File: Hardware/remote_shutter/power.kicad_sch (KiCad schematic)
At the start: 0 parts

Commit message: Added power & comms.
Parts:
- added C?: 10u, symbol Device:C_Polarized_Small
- added C?: 22u, symbol Device:C_Polarized_Small
- added J?: Conn_01x02_Male, symbol Connector:Conn_01x02_Male
- added U?: AZ1117-3.3, symbol Regulator_Linear:AZ1117-3.3
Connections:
- new net: C?.1, J?.1 (Pin_1), U?.3 (VI)
- new net 3V3: C?.1, U?.2 (VO)
- new net GND: C?.2, C?.2, J?.2 (Pin_2), U?.1 (GND)
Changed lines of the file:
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@@
 (kicad_sch (version 20211123) (generator eeschema)
   (paper "A4")
+  (junction (at 157.48 88.9) (diameter 0) (color 0 0 0 0)
+  )
+  (junction (at 132.08 88.9) (diameter 0) (color 0 0 0 0)
+  )
+  (wire (pts (xy 166.37 91.44) (xy 167.64 91.44))
+    (stroke (width 0) (type default) (color 0 0 0 0))
+  )
+  (wire (pts (xy 132.08 88.9) (xy 132.08 91.44))
+    (stroke (width 0) (type default) (color 0 0 0 0))
+  )
+  (wire (pts (xy 120.65 88.9) (xy 132.08 88.9))
+    (stroke (width 0) (type default) (color 0 0 0 0))
+  )
+  (wire (pts (xy 157.48 91.44) (xy 157.48 88.9))
+    (stroke (width 0) (type default) (color 0 0 0 0))
+  )
+  (wire (pts (xy 153.67 88.9) (xy 157.48 88.9))
+    (stroke (width 0) (type default) (color 0 0 0 0))
+  )
+  (wire (pts (xy 132.08 88.9) (xy 138.43 88.9))
+    (stroke (width 0) (type default) (color 0 0 0 0))
+  )
+  (wire (pts (xy 120.65 91.44) (xy 124.46 91.44))
+    (stroke (width 0) (type default) (color 0 0 0 0))
+  )
+  (wire (pts (xy 166.37 92.71) (xy 166.37 91.44))
+    (stroke (width 0) (type default) (color 0 0 0 0))
+  )
+  (wire (pts (xy 157.48 88.9) (xy 167.64 88.9))
+    (stroke (width 0) (type default) (color 0 0 0 0))
+  )
+  (hierarchical_label "3V3" (shape input) (at 167.64 88.9 0)
+    (effects (font (size 1.27 1.27)) (justify left))
+  )
+  (hierarchical_label "GND" (shape input) (at 167.64 91.44 0)
+    (effects (font (size 1.27 1.27)) (justify left))
+  )
+  (symbol (lib_id "power:GND") (at 166.37 92.71 0) (unit 1)
+    (in_bom yes) (on_board yes) (fields_autoplaced)
+    (property "Reference" "#PWR?" (id 0) (at 166.37 99.06 0)
+      (effects (font (size 1.27 1.27)) hide)
+    )
+    (property "Value" "GND" (id 1) (at 166.37 97.79 0))
+    (property "Footprint" "" (id 2) (at 166.37 92.71 0)
+      (effects (font (size 1.27 1.27)) hide)
+    )
+    (property "Datasheet" "" (id 3) (at 166.37 92.71 0)
+      (effects (font (size 1.27 1.27)) hide)
+    )
+    (pin "1")
+  )
+  (symbol (lib_id "power:GND") (at 132.08 96.52 0) (unit 1)
+    (in_bom yes) (on_board yes) (fields_autoplaced)
+    (property "Reference" "#PWR?" (id 0) (at 132.08 102.87 0)
+      (effects (font (size 1.27 1.27)) hide)
+    )
+    (property "Value" "GND" (id 1) (at 132.08 101.6 0))
+    (property "Footprint" "" (id 2) (at 132.08 96.52 0)
+      (effects (font (size 1.27 1.27)) hide)
+    )
+    (property "Datasheet" "" (id 3) (at 132.08 96.52 0)
+      (effects (font (size 1.27 1.27)) hide)
+    )
+    (pin "1")
+  )
+  (symbol (lib_id "Device:C_Polarized_Small") (at 132.08 93.98 0) (unit 1)
+    (in_bom yes) (on_board yes) (fields_autoplaced)
+    (property "Reference" "C?" (id 0) (at 134.62 92.1638 0)
+      (effects (font (size 1.27 1.27)) (justify left))
+    )
+    (property "Value" "10u" (id 1) (at 134.62 94.7038 0)
+      (effects (font (size 1.27 1.27)) (justify left))
+    )
+    (property "Footprint" "" (id 2) (at 132.08 93.98 0)
+      (effects (font (size 1.27 1.27)) hide)
+    )
+    (property "Datasheet" "~" (id 3) (at 132.08 93.98 0)
+      (effects (font (size 1.27 1.27)) hide)
+    )
+    (pin "1")
+    (pin "2")
+  )
+  (symbol (lib_id "power:GND") (at 124.46 91.44 0) (unit 1)
+    (in_bom yes) (on_board yes) (fields_autoplaced)
+    (property "Reference" "#PWR?" (id 0) (at 124.46 97.79 0)
+      (effects (font (size 1.27 1.27)) hide)
+    )
+    (property "Value" "GND" (id 1) (at 124.46 96.52 0))
+    (property "Footprint" "" (id 2) (at 124.46 91.44 0)
+      (effects (font (size 1.27 1.27)) hide)
+    )
+    (property "Datasheet" "" (id 3) (at 124.46 91.44 0)
+      (effects (font (size 1.27 1.27)) hide)
+    )
+    (pin "1")
+  )
+  (symbol (lib_id "power:GND") (at 146.05 96.52 0) (unit 1)
+    (in_bom yes) (on_board yes) (fields_autoplaced)
+    (property "Reference" "#PWR?" (id 0) (at 146.05 102.87 0)
+      (effects (font (size 1.27 1.27)) hide)
+    )
+    (property "Value" "GND" (id 1) (at 146.05 101.6 0))
+    (property "Footprint" "" (id 2) (at 146.05 96.52 0)
+      (effects (font (size 1.27 1.27)) hide)
+    )
+    (property "Datasheet" "" (id 3) (at 146.05 96.52 0)
+      (effects (font (size 1.27 1.27)) hide)
+    )
+    (pin "1")
+  )
+  (symbol (lib_id "Regulator_Linear:AZ1117-3.3") (at 146.05 88.9 0) (unit 1)
+    (in_bom yes) (on_board yes) (fields_autoplaced)
+    (property "Reference" "U?" (id 0) (at 146.05 81.28 0))
+    (property "Value" "AZ1117-3.3" (id 1) (at 146.05 83.82 0))
+    (property "Footprint" "" (id 2) (at 146.05 82.55 0)
+      (effects (font (size 1.27 1.27) italic) hide)
+    )
+    (property "Datasheet" "https://www.diodes.com/assets/Datasheets/AZ1117.pdf" (id 3) (at 146.05 88.9 0)
+      (effects (font (size 1.27 1.27)) hide)
+    )
+    (pin "1")
+    (pin "2")
+    (pin "3")
+  )
+  (symbol (lib_id "power:GND") (at 157.48 96.52 0) (unit 1)
+    (in_bom yes) (on_board yes) (fields_autoplaced)
+    (property "Reference" "#PWR?" (id 0) (at 157.48 102.87 0)
+      (effects (font (size 1.27 1.27)) hide)
+    )
+    (property "Value" "GND" (id 1) (at 157.48 101.6 0))
+    (property "Footprint" "" (id 2) (at 157.48 96.52 0)
+      (effects (font (size 1.27 1.27)) hide)
+    )
+    (property "Datasheet" "" (id 3) (at 157.48 96.52 0)
+      (effects (font (size 1.27 1.27)) hide)
+    )
+    (pin "1")
+  )
+  (symbol (lib_id "Device:C_Polarized_Small") (at 157.48 93.98 0) (unit 1)
+    (in_bom yes) (on_board yes) (fields_autoplaced)
+    (property "Reference" "C?" (id 0) (at 160.02 92.1638 0)
+      (effects (font (size 1.27 1.27)) (justify left))
+    )
+    (property "Value" "22u" (id 1) (at 160.02 94.7038 0)
+      (effects (font (size 1.27 1.27)) (justify left))
+    )
+    (property "Footprint" "" (id 2) (at 157.48 93.98 0)
+      (effects (font (size 1.27 1.27)) hide)
+    )
+    (property "Datasheet" "~" (id 3) (at 157.48 93.98 0)
+      (effects (font (size 1.27 1.27)) hide)
+    )
+    (pin "1")
+    (pin "2")
+  )
+  (symbol (lib_id "Connector:Conn_01x02_Male") (at 115.57 88.9 0) (unit 1)
+    (in_bom yes) (on_board yes) (fields_autoplaced)
+    (property "Reference" "J?" (id 0) (at 116.205 83.82 0))
+    (property "Value" "Conn_01x02_Male" (id 1) (at 116.205 86.36 0))
+    (property "Footprint" "" (id 2) (at 115.57 88.9 0)
+      (effects (font (size 1.27 1.27)) hide)
+    )
+    (property "Datasheet" "~" (id 3) (at 115.57 88.9 0)
+      (effects (font (size 1.27 1.27)) hide)
+    )
+    (pin "1")
+    (pin "2")
+  )
 )

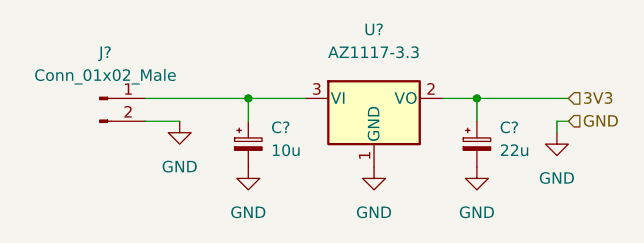
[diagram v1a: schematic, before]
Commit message: Added missing footprints. First PCB export.
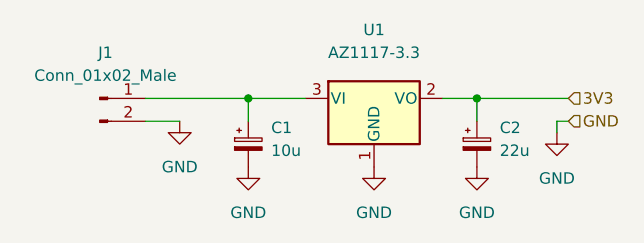
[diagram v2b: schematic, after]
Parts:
- C1, C2: renamed from C?; footprint (none) -> Capacitor_Tantalum_SMD:CP_EIA-3528-21_Kemet-B_Pad1.50x2.35mm_HandSolder
- gave numbers to parts that had none: 2
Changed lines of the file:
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@@
   (symbol (lib_id "power:GND") (at 166.37 92.71 0) (unit 1)
     (in_bom yes) (on_board yes) (fields_autoplaced)
-    (property "Reference" "#PWR?" (id 0) (at 166.37 99.06 0)
+    (property "Reference" "#PWR0102" (id 0) (at 166.37 99.06 0)
       (effects (font (size 1.27 1.27)) hide)
     )
@@
   (symbol (lib_id "power:GND") (at 132.08 96.52 0) (unit 1)
     (in_bom yes) (on_board yes) (fields_autoplaced)
-    (property "Reference" "#PWR?" (id 0) (at 132.08 102.87 0)
+    (property "Reference" "#PWR0104" (id 0) (at 132.08 102.87 0)
       (effects (font (size 1.27 1.27)) hide)
     )
@@
   (symbol (lib_id "Device:C_Polarized_Small") (at 132.08 93.98 0) (unit 1)
     (in_bom yes) (on_board yes) (fields_autoplaced)
-    (property "Reference" "C?" (id 0) (at 134.62 92.1638 0)
+    (property "Reference" "C1" (id 0) (at 134.62 92.1638 0)
       (effects (font (size 1.27 1.27)) (justify left))
     )
@@
       (effects (font (size 1.27 1.27)) (justify left))
     )
-    (property "Footprint" "" (id 2) (at 132.08 93.98 0)
+    (property "Footprint" "Capacitor_Tantalum_SMD:CP_EIA-3528-21_Kemet-B_Pad1.50x2.35mm_HandSolder" (id 2) (at 132.08 93.98 0)
       (effects (font (size 1.27 1.27)) hide)
     )
@@
   (symbol (lib_id "power:GND") (at 124.46 91.44 0) (unit 1)
     (in_bom yes) (on_board yes) (fields_autoplaced)
-    (property "Reference" "#PWR?" (id 0) (at 124.46 97.79 0)
+    (property "Reference" "#PWR0105" (id 0) (at 124.46 97.79 0)
       (effects (font (size 1.27 1.27)) hide)
     )
@@
   (symbol (lib_id "power:GND") (at 146.05 96.52 0) (unit 1)
     (in_bom yes) (on_board yes) (fields_autoplaced)
-    (property "Reference" "#PWR?" (id 0) (at 146.05 102.87 0)
+    (property "Reference" "#PWR0103" (id 0) (at 146.05 102.87 0)
       (effects (font (size 1.27 1.27)) hide)
     )
@@
   (symbol (lib_id "Regulator_Linear:AZ1117-3.3") (at 146.05 88.9 0) (unit 1)
     (in_bom yes) (on_board yes) (fields_autoplaced)
-    (property "Reference" "U?" (id 0) (at 146.05 81.28 0))
+    (property "Reference" "U1" (id 0) (at 146.05 81.28 0))
     (property "Value" "AZ1117-3.3" (id 1) (at 146.05 83.82 0))
     (property "Footprint" "" (id 2) (at 146.05 82.55 0)
@@
   (symbol (lib_id "power:GND") (at 157.48 96.52 0) (unit 1)
     (in_bom yes) (on_board yes) (fields_autoplaced)
-    (property "Reference" "#PWR?" (id 0) (at 157.48 102.87 0)
+    (property "Reference" "#PWR0101" (id 0) (at 157.48 102.87 0)
       (effects (font (size 1.27 1.27)) hide)
     )
@@
   (symbol (lib_id "Device:C_Polarized_Small") (at 157.48 93.98 0) (unit 1)
     (in_bom yes) (on_board yes) (fields_autoplaced)
-    (property "Reference" "C?" (id 0) (at 160.02 92.1638 0)
+    (property "Reference" "C2" (id 0) (at 160.02 92.1638 0)
       (effects (font (size 1.27 1.27)) (justify left))
     )
@@
       (effects (font (size 1.27 1.27)) (justify left))
     )
-    (property "Footprint" "" (id 2) (at 157.48 93.98 0)
+    (property "Footprint" "Capacitor_Tantalum_SMD:CP_EIA-3528-21_Kemet-B_Pad1.50x2.35mm_HandSolder" (id 2) (at 157.48 93.98 0)
       (effects (font (size 1.27 1.27)) hide)
     )
@@
   (symbol (lib_id "Connector:Conn_01x02_Male") (at 115.57 88.9 0) (unit 1)
     (in_bom yes) (on_board yes) (fields_autoplaced)
-    (property "Reference" "J?" (id 0) (at 116.205 83.82 0))
+    (property "Reference" "J1" (id 0) (at 116.205 83.82 0))
     (property "Value" "Conn_01x02_Male" (id 1) (at 116.205 86.36 0))
     (property "Footprint" "" (id 2) (at 115.57 88.9 0)

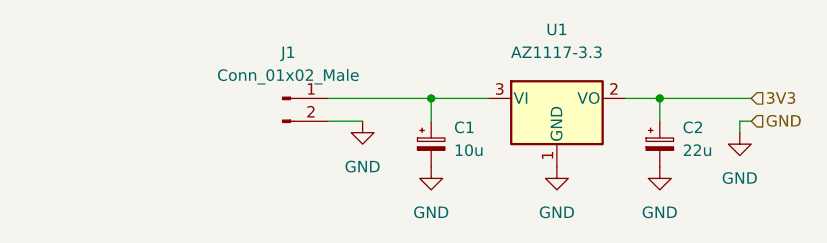
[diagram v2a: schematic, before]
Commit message: Started routing. Added power switch.
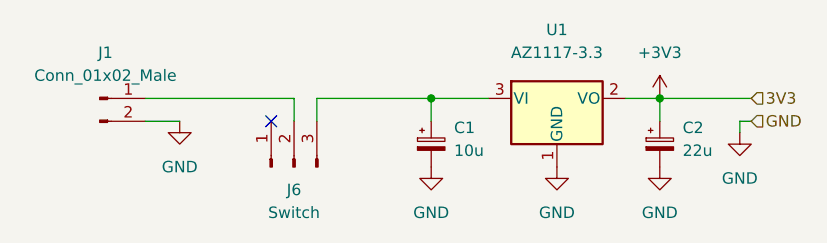
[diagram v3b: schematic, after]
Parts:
- added J6: Switch, Connector_PinHeader_2.54mm:PinHeader_1x03_P2.54mm_Vertical, symbol Connector:Conn_01x03_Male
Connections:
- net at C1.1, U1.3 (VI): now also J6.3 (Pin_3); no longer J1.1 (Pin_1)
- net 3V3 renamed +3V3
- new net: J1.1 (Pin_1), J6.2 (Pin_2)
- no-connect marks 0 -> 1
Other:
- moved on the sheet: J1
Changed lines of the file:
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@@
   (junction (at 132.08 88.9) (diameter 0) (color 0 0 0 0)
   )
+  (no_connect (at 114.3 91.44))
+  (wire (pts (xy 119.38 88.9) (xy 132.08 88.9))
+    (stroke (width 0) (type default) (color 0 0 0 0))
+  )
   (wire (pts (xy 166.37 91.44) (xy 167.64 91.44))
     (stroke (width 0) (type default) (color 0 0 0 0))
@@
     (stroke (width 0) (type default) (color 0 0 0 0))
   )
-  (wire (pts (xy 120.65 88.9) (xy 132.08 88.9))
-    (stroke (width 0) (type default) (color 0 0 0 0))
-  )
   (wire (pts (xy 157.48 91.44) (xy 157.48 88.9))
     (stroke (width 0) (type default) (color 0 0 0 0))
   )
+  (wire (pts (xy 116.84 88.9) (xy 116.84 91.44))
+    (stroke (width 0) (type default) (color 0 0 0 0))
+  )
   (wire (pts (xy 153.67 88.9) (xy 157.48 88.9))
     (stroke (width 0) (type default) (color 0 0 0 0))
@@
     (stroke (width 0) (type default) (color 0 0 0 0))
   )
-  (wire (pts (xy 120.65 91.44) (xy 124.46 91.44))
+  (wire (pts (xy 100.33 91.44) (xy 104.14 91.44))
     (stroke (width 0) (type default) (color 0 0 0 0))
   )
   (wire (pts (xy 166.37 92.71) (xy 166.37 91.44))
+    (stroke (width 0) (type default) (color 0 0 0 0))
+  )
+  (wire (pts (xy 100.33 88.9) (xy 116.84 88.9))
+    (stroke (width 0) (type default) (color 0 0 0 0))
+  )
+  (wire (pts (xy 119.38 91.44) (xy 119.38 88.9))
     (stroke (width 0) (type default) (color 0 0 0 0))
   )
@@
     (effects (font (size 1.27 1.27)) (justify left))
   )
+  (symbol (lib_id "power:+3V3") (at 157.48 88.9 0) (unit 1)
+    (in_bom yes) (on_board yes) (fields_autoplaced)
+    (property "Reference" "#PWR?" (id 0) (at 157.48 92.71 0)
+      (effects (font (size 1.27 1.27)) hide)
+    )
+    (property "Value" "+3V3" (id 1) (at 157.48 83.82 0))
+    (property "Footprint" "" (id 2) (at 157.48 88.9 0)
+      (effects (font (size 1.27 1.27)) hide)
+    )
+    (property "Datasheet" "" (id 3) (at 157.48 88.9 0)
+      (effects (font (size 1.27 1.27)) hide)
+    )
+    (pin "1")
+  )
   (symbol (lib_id "power:GND") (at 166.37 92.71 0) (unit 1)
     (in_bom yes) (on_board yes) (fields_autoplaced)
@@
     (pin "2")
   )
-  (symbol (lib_id "power:GND") (at 124.46 91.44 0) (unit 1)
-    (in_bom yes) (on_board yes) (fields_autoplaced)
-    (property "Reference" "#PWR0105" (id 0) (at 124.46 97.79 0)
-      (effects (font (size 1.27 1.27)) hide)
-    )
-    (property "Value" "GND" (id 1) (at 124.46 96.52 0))
-    (property "Footprint" "" (id 2) (at 124.46 91.44 0)
-      (effects (font (size 1.27 1.27)) hide)
-    )
-    (property "Datasheet" "" (id 3) (at 124.46 91.44 0)
+  (symbol (lib_id "power:GND") (at 104.14 91.44 0) (unit 1)
+    (in_bom yes) (on_board yes) (fields_autoplaced)
+    (property "Reference" "#PWR0105" (id 0) (at 104.14 97.79 0)
+      (effects (font (size 1.27 1.27)) hide)
+    )
+    (property "Value" "GND" (id 1) (at 104.14 96.52 0))
+    (property "Footprint" "" (id 2) (at 104.14 91.44 0)
+      (effects (font (size 1.27 1.27)) hide)
+    )
+    (property "Datasheet" "" (id 3) (at 104.14 91.44 0)
       (effects (font (size 1.27 1.27)) hide)
     )
@@
     (pin "2")
   )
-  (symbol (lib_id "Connector:Conn_01x02_Male") (at 115.57 88.9 0) (unit 1)
-    (in_bom yes) (on_board yes) (fields_autoplaced)
-    (property "Reference" "J1" (id 0) (at 116.205 83.82 0))
-    (property "Value" "Conn_01x02_Male" (id 1) (at 116.205 86.36 0))
-    (property "Footprint" "" (id 2) (at 115.57 88.9 0)
-      (effects (font (size 1.27 1.27)) hide)
-    )
-    (property "Datasheet" "~" (id 3) (at 115.57 88.9 0)
-      (effects (font (size 1.27 1.27)) hide)
-    )
+  (symbol (lib_id "Connector:Conn_01x03_Male") (at 116.84 96.52 90) (unit 1)
+    (in_bom yes) (on_board yes) (fields_autoplaced)
+    (property "Reference" "J6" (id 0) (at 116.84 99.06 90))
+    (property "Value" "Switch" (id 1) (at 116.84 101.6 90))
+    (property "Footprint" "Connector_PinHeader_2.54mm:PinHeader_1x03_P2.54mm_Vertical" (id 2) (at 116.84 96.52 0)
+      (effects (font (size 1.27 1.27)) hide)
+    )
+    (property "Datasheet" "~" (id 3) (at 116.84 96.52 0)
+      (effects (font (size 1.27 1.27)) hide)
+    )
+    (pin "1")
+    (pin "2")
+    (pin "3")
+  )
+  (symbol (lib_id "Connector:Conn_01x02_Male") (at 95.25 88.9 0) (unit 1)
+    (in_bom yes) (on_board yes) (fields_autoplaced)
+    (property "Reference" "J1" (id 0) (at 95.885 83.82 0))
+    (property "Value" "Conn_01x02_Male" (id 1) (at 95.885 86.36 0))
+    (property "Footprint" "" (id 2) (at 95.25 88.9 0)
+      (effects (font (size 1.27 1.27)) hide)
+    )
+    (property "Datasheet" "~" (id 3) (at 95.25 88.9 0)
+      (effects (font (size 1.27 1.27)) hide)
+    )

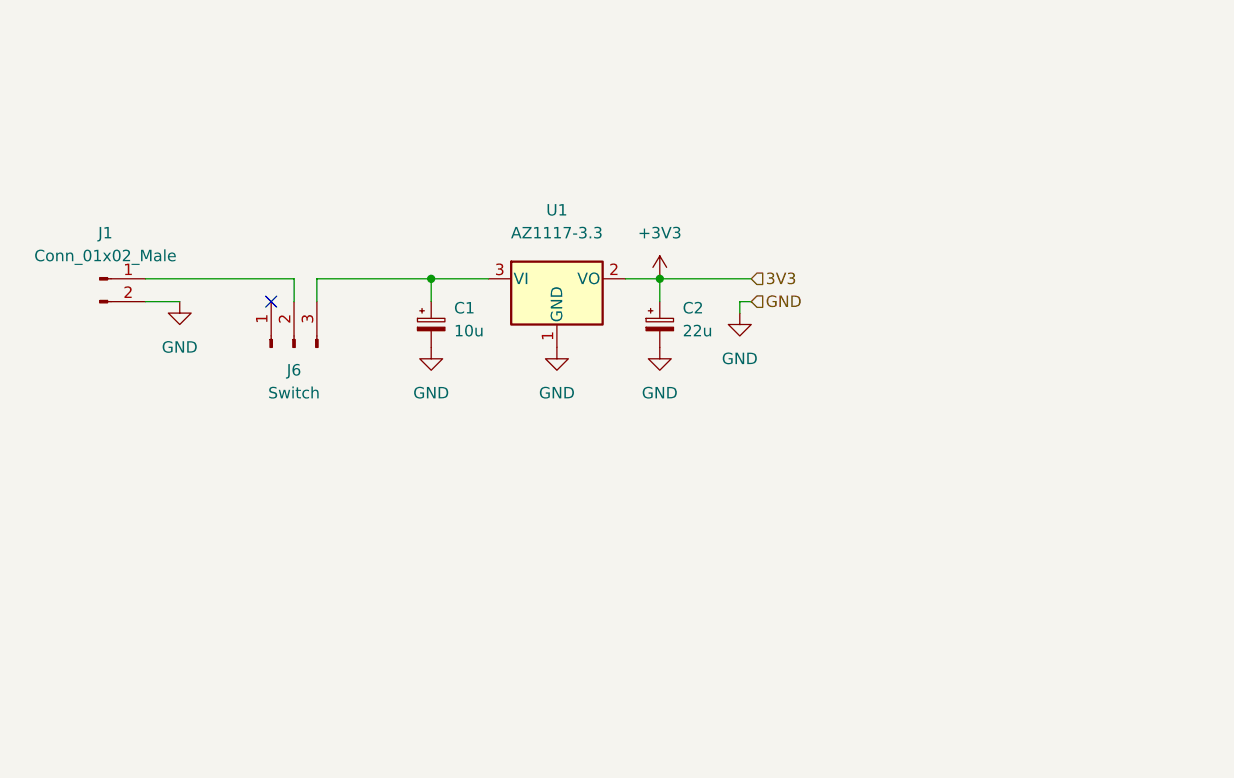
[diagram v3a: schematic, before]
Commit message: Added LiIon charge circuit
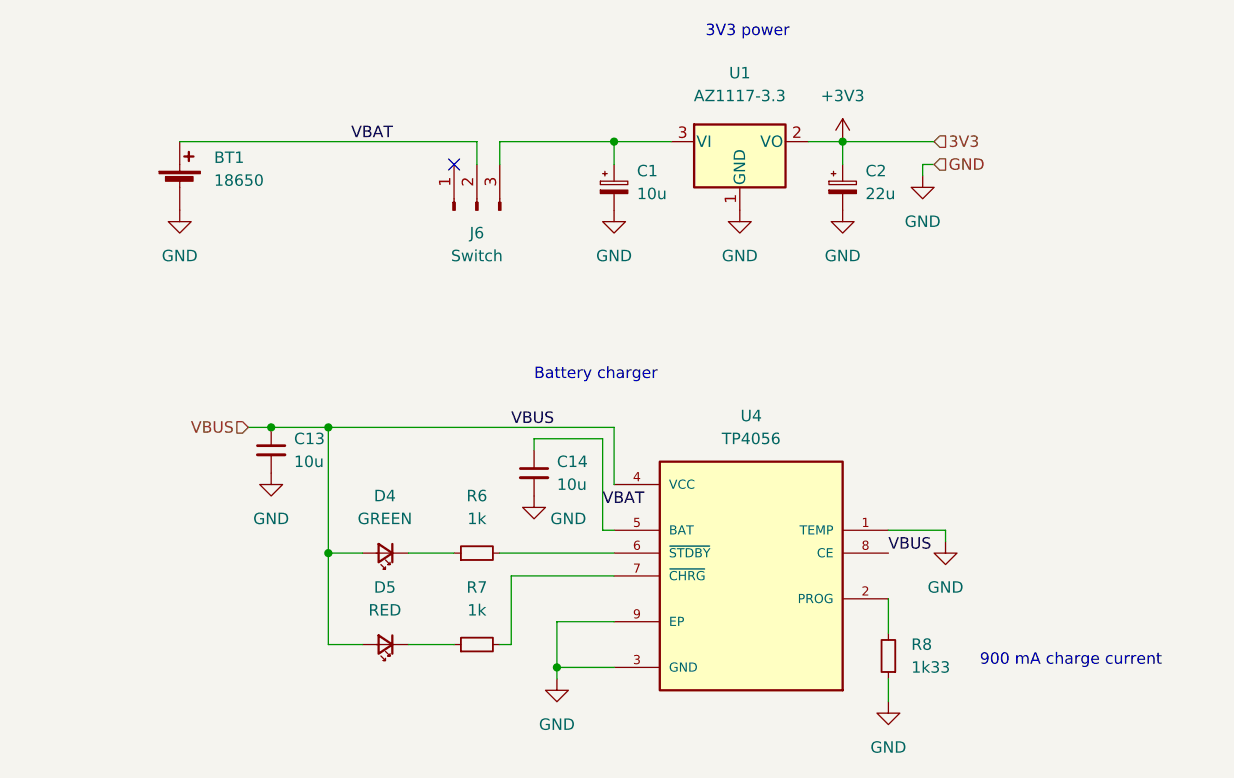
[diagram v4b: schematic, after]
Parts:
- removed J1: Conn_01x02_Male, symbol Connector:Conn_01x02_Male
- added BT1: 18650, Connector_PinHeader_2.54mm:PinHeader_1x02_P2.54mm_Vertical, symbol Device:Battery_Cell
- added C13, C14: 10u, Capacitor_SMD:C_0805_2012Metric_Pad1.18x1.45mm_HandSolder, symbol Device:C_Small
- added D4: GREEN, LED_SMD:LED_0603_1608Metric_Pad1.05x0.95mm_HandSolder, symbol Device:LED_Small
- added D5: RED, LED_SMD:LED_0603_1608Metric_Pad1.05x0.95mm_HandSolder, symbol Device:LED_Small
- added R6, R7: 1k, Resistor_SMD:R_0603_1608Metric_Pad0.98x0.95mm_HandSolder, symbol Device:R_Small
- added R8: 1k33, Resistor_SMD:R_0603_1608Metric_Pad0.98x0.95mm_HandSolder, symbol Device:R_Small
- added U4: TP4056, footprint:SOP127P600X175-9N, symbol TP4056:TP4056
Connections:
- net GND: now also BT1.2 (-), C13.2, C14.2, R8.1, U4.1 (TEMP), U4.3 (GND), U4.9 (EP)
- net VBAT: now reaches J6.2 (Pin_2)
- net VBAT: now also BT1.1 (+), C14.1, U4.5 (BAT)
- new net: D4.1 (K), R6.1
- new net: D5.1 (K), R7.1
- new net: R7.2, U4.7 (~{CHRG})
- new net: R6.2, U4.6 (~{STDBY})
- new net: R8.2, U4.2 (PROG)
- new net VBUS: C13.1, D4.2 (A), D5.2 (A), U4.4 (VCC), U4.8 (CE)
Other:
- note added: "3V3 power"
- note added: "900 mA charge current"
- note added: "Battery charger"
- moved on the sheet: C1, C2, J6, U1

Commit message: Fixed via sizes. Added IO0 pullup.
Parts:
- U1: footprint (none) -> Package_TO_SOT_SMD:SOT-223-3_TabPin2
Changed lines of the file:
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@@
     (property "Reference" "U1" (id 0) (at 166.37 66.04 0))
     (property "Value" "AZ1117-3.3" (id 1) (at 166.37 68.58 0))
-    (property "Footprint" "" (id 2) (at 166.37 67.31 0)
+    (property "Footprint" "Package_TO_SOT_SMD:SOT-223-3_TabPin2" (id 2) (at 166.37 67.31 0)
       (effects (font (size 1.27 1.27) italic) hide)
     )
